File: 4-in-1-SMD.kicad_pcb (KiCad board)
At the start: 2 copper layers, 100 x 100 mm, 46 parts

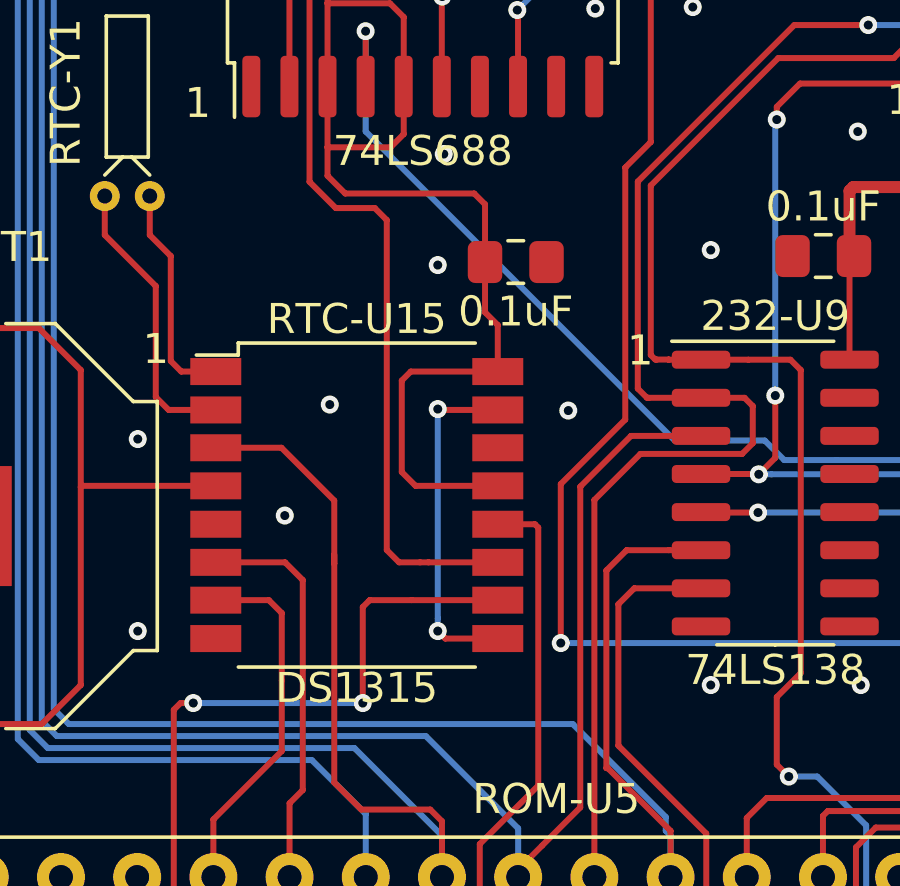
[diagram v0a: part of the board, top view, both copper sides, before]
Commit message: RTC Bypass Jumper
Adds solder jumper for omission of Smartwatch RTC parts.
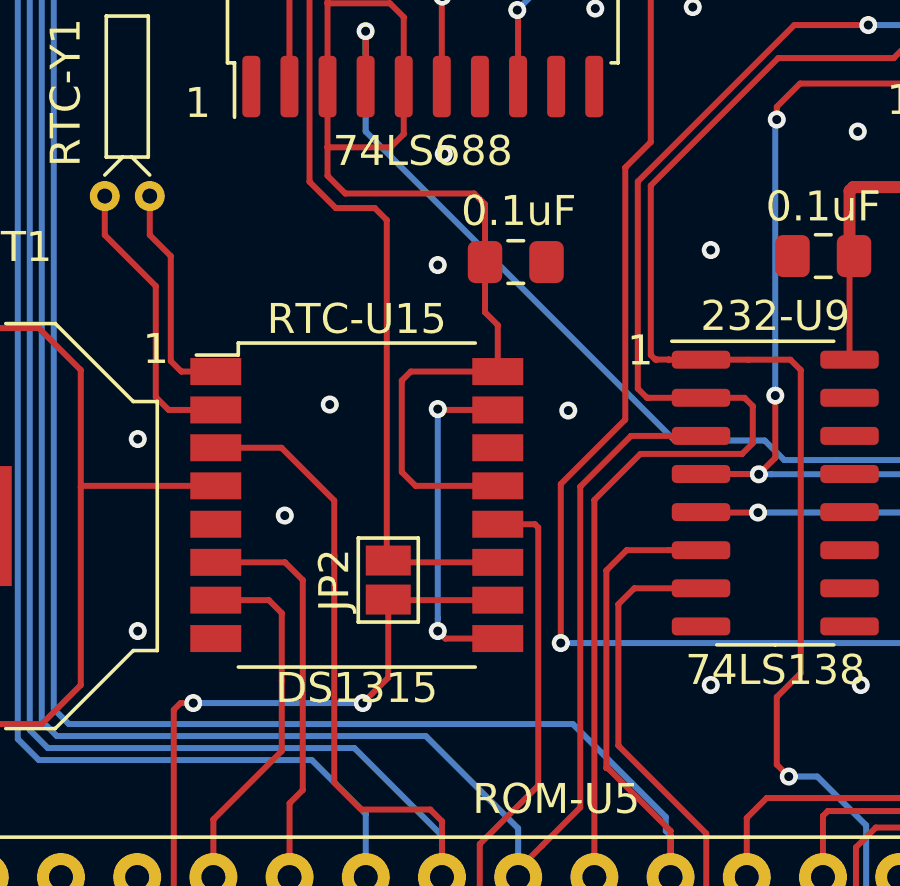
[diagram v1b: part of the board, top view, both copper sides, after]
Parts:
- added JP2: No-RTC Enable, Jumper:SolderJumper-2_P1.3mm_Open_Pad1.0x1.5mm, F.Cu at (122.8, 71.5)

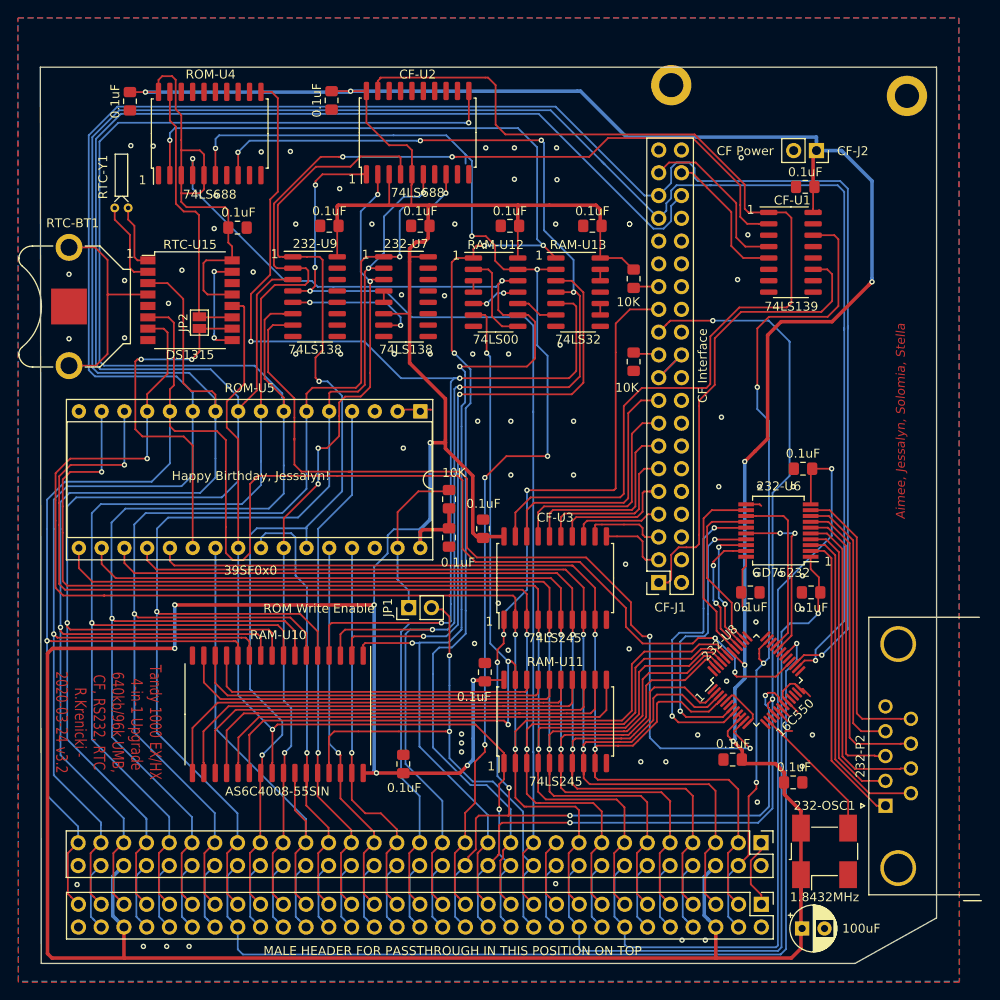
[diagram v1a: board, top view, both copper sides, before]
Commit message: Update to KiCAD 9.0
Updated to KiCAD 9.0.  Regenerated Gerber for missing JP2
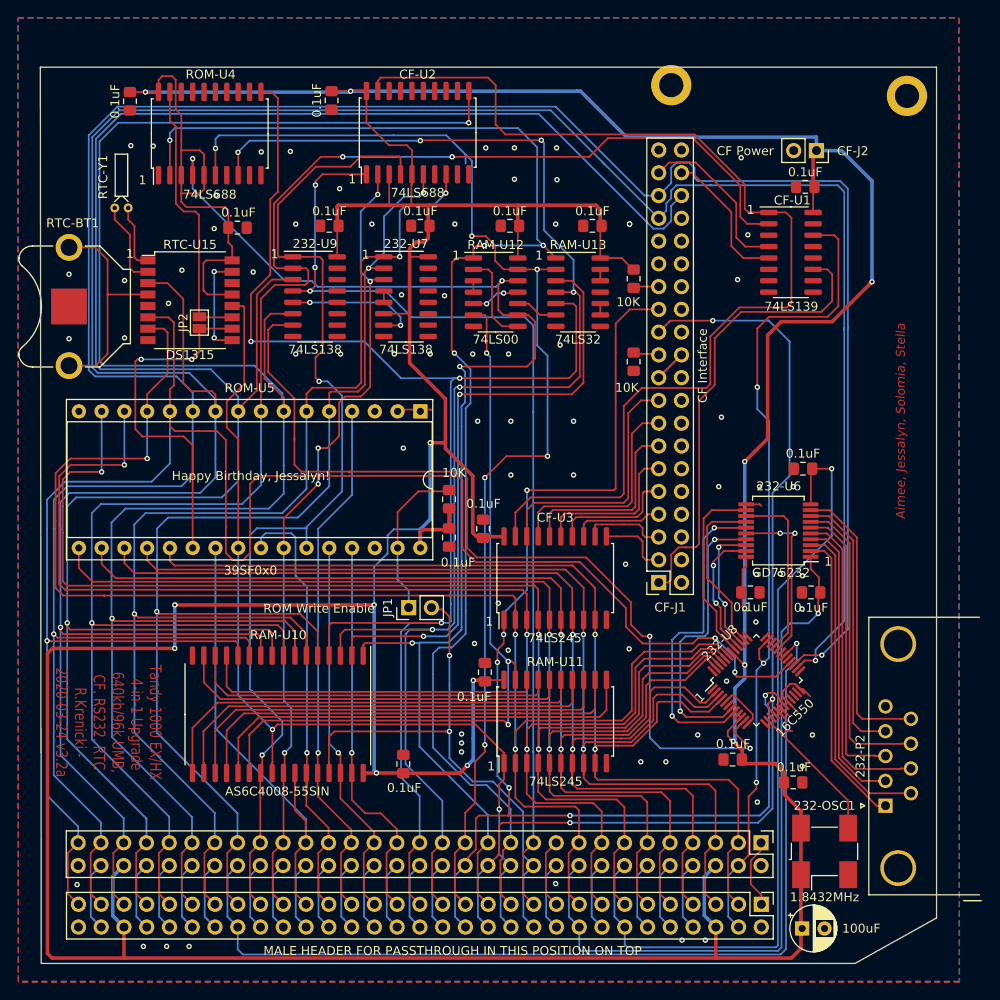
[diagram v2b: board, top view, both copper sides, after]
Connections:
- net ~IOR renamed ~{IOR}
- net ~IOW renamed ~{IOW}
- net ~MEMR renamed ~{MEMR}
- net ~MEMW renamed ~{MEMW}
- net ~ROM_CS renamed ~{ROM_CS}
- net ~RTC_CS renamed ~{RTC_CS}
- net ~UART_CS renamed ~{UART_CS}
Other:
- net class Default removed
- board text added: "Tandy 1000 EX/HX 4-in-1 Upgrade 640kb/96k UMB, CF, RS232, RTC R.Krenicki - 2020-03-24 v3.2a"
- board text removed: "Tandy 1000 EX/HX 4-in-1 Upgrade 640kb/96k UMB, CF, RS232, RTC R.Krenicki - 2020-03-24 v3.2"
